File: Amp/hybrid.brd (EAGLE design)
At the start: 174 x 168.9 mm, 123 parts, among them IC1 TL071P, IC2 TL071P, IC3 LM317MABT-OUT, IC4 LM317MABT-OUT, J1 RCJ-21XXMILL, J2 NRJ3HF-1, J3 703W-00/54, Q1 BC560KINKED, Q10 BC560KINKED, Q11 BC560KINKED, Q12 BC560KINKED, Q13 BC556KINKED, Q14 BC550KINKED, Q15 BC550KINKED, Q16 BC560KINKED, Q17 BD140, Q18 BD139, Q19 KSP43, Q2 BC560KINKED, Q3 BC560KINKED, Q4 BC556KINKED, Q5 BC550KINKED, Q6 BC550KINKED, Q7 BC560KINKED, Q8 BD140, Q9 BD139, T1 TR-LP30-1600

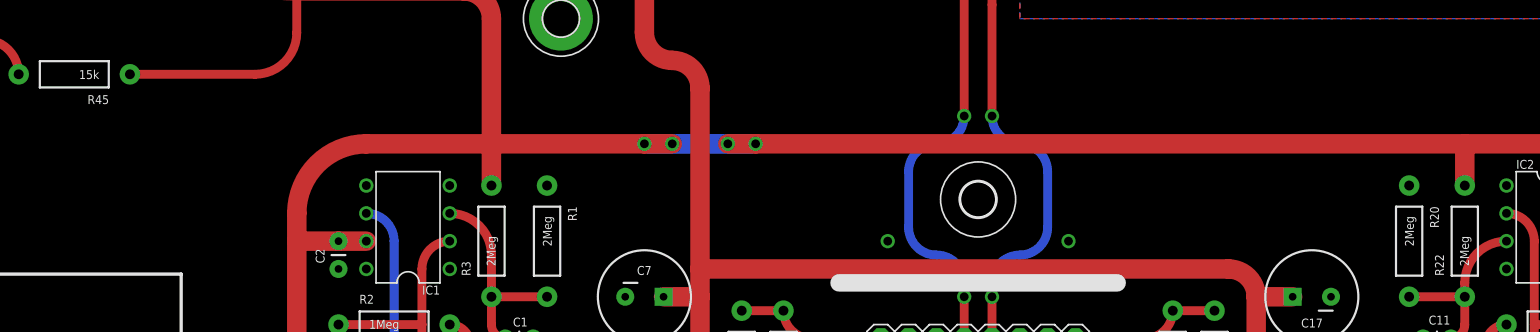
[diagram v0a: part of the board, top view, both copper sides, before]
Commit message: Improved auto biasing circuit
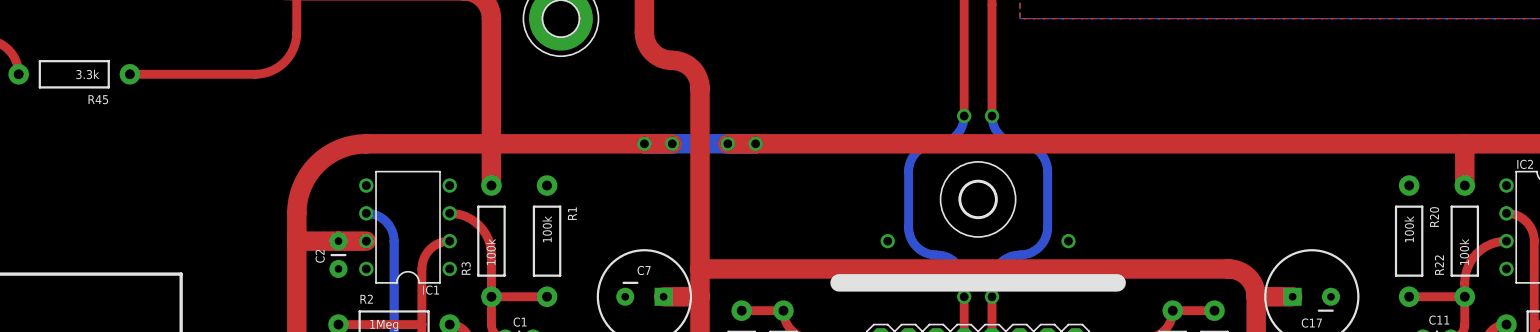
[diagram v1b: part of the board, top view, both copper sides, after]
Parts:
- R1, R20, R22, R3: value 2Meg -> 100k
- R45: value 15k -> 3.3k
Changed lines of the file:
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@@
 <?xml version="1.0" encoding="utf-8"?>
 <!DOCTYPE eagle SYSTEM "eagle.dtd">
-<eagle version="8.0.2">
+<eagle version="8.1.0">
 <drawing>
 <settings>
@@
 <attribute name="VALUE" x="46.355" y="1.143" size="0.8128" layer="27" ratio="20" rot="R180"/>
 </element>
-<element name="R1" library="SparkFun-Resistors" package="AXIAL-0.4" value="2Meg" x="57.15" y="67.31" smashed="yes" rot="R270">
+<element name="R1" library="SparkFun-Resistors" package="AXIAL-0.4" value="100k" x="57.15" y="67.31" smashed="yes" rot="R270">
 <attribute name="NAME" x="59.055" y="70.485" size="0.8128" layer="25" font="vector" ratio="20" rot="R270"/>
 <attribute name="VALUE" x="56.769" y="69.596" size="0.8128" layer="21" font="vector" ratio="20" rot="R270"/>
@@
 <attribute name="VALUE" x="37.719" y="26.416" size="0.8128" layer="21" font="vector" ratio="20" rot="R270"/>
 </element>
-<element name="R20" library="SparkFun-Resistors" package="AXIAL-0.4" value="2Meg" x="135.89" y="67.31" smashed="yes" rot="R270">
+<element name="R20" library="SparkFun-Resistors" package="AXIAL-0.4" value="100k" x="135.89" y="67.31" smashed="yes" rot="R270">
 <attribute name="NAME" x="137.795" y="70.485" size="0.8128" layer="25" font="vector" ratio="20" rot="R270"/>
 <attribute name="VALUE" x="135.509" y="69.596" size="0.8128" layer="21" font="vector" ratio="20" rot="R270"/>
@@
 <attribute name="VALUE" x="152.146" y="60.071" size="0.8128" layer="21" font="vector" ratio="20" rot="R180"/>
 </element>
-<element name="R22" library="SparkFun-Resistors" package="AXIAL-0.4" value="2Meg" x="140.97" y="67.31" smashed="yes" rot="R90">
+<element name="R22" library="SparkFun-Resistors" package="AXIAL-0.4" value="100k" x="140.97" y="67.31" smashed="yes" rot="R90">
 <attribute name="NAME" x="139.065" y="64.135" size="0.8128" layer="25" font="vector" ratio="20" rot="R90"/>
 <attribute name="VALUE" x="141.351" y="65.024" size="0.8128" layer="21" font="vector" ratio="20" rot="R90"/>
@@
 <attribute name="VALUE" x="154.559" y="26.416" size="0.8128" layer="21" font="vector" ratio="20" rot="R270"/>
 </element>
-<element name="R3" library="SparkFun-Resistors" package="AXIAL-0.4" value="2Meg" x="52.07" y="67.31" smashed="yes" rot="R90">
+<element name="R3" library="SparkFun-Resistors" package="AXIAL-0.4" value="100k" x="52.07" y="67.31" smashed="yes" rot="R90">
 <attribute name="NAME" x="50.165" y="64.135" size="0.8128" layer="25" font="vector" ratio="20" rot="R90"/>
 <attribute name="VALUE" x="52.451" y="65.024" size="0.8128" layer="21" font="vector" ratio="20" rot="R90"/>
@@
 <attribute name="VALUE" x="2.159" y="82.55" size="1.27" layer="27" ratio="10" rot="R270"/>
 </element>
-<element name="R45" library="SparkFun-Resistors" package="AXIAL-0.4" value="15k" x="13.97" y="82.55" smashed="yes" rot="R180">
+<element name="R45" library="SparkFun-Resistors" package="AXIAL-0.4" value="3.3k" x="13.97" y="82.55" smashed="yes" rot="R180">
 <attribute name="NAME" x="17.145" y="80.645" size="0.8128" layer="25" font="vector" ratio="20" rot="R180"/>
 <attribute name="VALUE" x="16.256" y="82.931" size="0.8128" layer="21" font="vector" ratio="20" rot="R180"/>

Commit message: Small changes
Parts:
- removed C30: 1uF, SparkFun-Capacitors:CAP-PTH-SMALL
- removed C31, C32: 47uF, my-cap:CPOL-RADIAL-8/3.5
- removed F1: (no value), fuse:SH22,5
- removed J1: RCJ-21XXMILL, my:RCJ-21-MILL
- removed J3: 703W-00/54, my-conn:703W-00/54
- removed S1: SW-M2012SA2W40, my-sw:SW-M2012S2A2G40
- removed T1: TR-LP30-1600, my-transformers:TR-LP30-1600
- removed U$1: ACRIDA-LOGO, my-logo:ACRIDA-LOGO
- removed U$2: (no value), my-logo:DANGER-LOGO
- added C25: 10uF, my-cap:CPOL-RADIAL-6.5/2.5
- added H1: MOUNT-PAD-ROUND3.2, holes:3,2-PAD
- added H6: MOUNT-HOLE3.2, holes:3,2
- added LOGO1: ACRIDA-LOGO, my-logo:ACRIDA-LOGO
- added Q20: BD139, transistor-npn:TO126
- added Q21, Q22: KSP43, my-tran:TO-92
- added R46: 23.7k, SparkFun-Resistors:AXIAL-0.4
- added R47: 3.3k, SparkFun-Resistors:AXIAL-0.4
- added R48: 220, SparkFun-Resistors:AXIAL-0.4
- added X1: (no value), con-wago-508:W237-3E
- added X2: (no value), con-wago-508:W237-2N
- C1, C11: value 0.1uF -> 1uF; device SparkFun-Capacitors:CAP-PTH-SMALL -> capacitor-wima:C5B5
- C10: value 470uF -> 1uF; device my-cap:CPOL-RADIAL-12.5/5 -> capacitor-wima:C5B5
- C12, C2: value 0.1uF -> 1uF
- C13: value 1uF -> 0.33u; device capacitor-wima:C5B5 -> capacitor-wima:C5B7.2
- C14: value 0.33u -> 100uF; device capacitor-wima:C5B3.5 -> my-cap:CPOL-RADIAL-8/3.5
- C15: value 10p -> 100uF; device SparkFun-Capacitors:CAP-PTH-SMALL -> my-cap:CPOL-RADIAL-12.5/5
- C16, C6: device my-cap:CPOL-RADIAL-8/3.5 -> my-cap:CPOL-RADIAL-12.5/5
- C17, C18, C8: value 47uF -> 470uF; device my-cap:CPOL-RADIAL-8/3.5 -> my-cap:CPOL-RADIAL-12.5/5
- C19, C20: device my-cap:CPOL-RADIAL-12.5/5 -> my-cap:CPOL-RADIAL-18/7.5
- C21: value 470uF -> 4700uF; device my-cap:CPOL-RADIAL-18/7.5 -> my-cap:CPOL-SNAPIN-30/10
- C22: value 470uF -> 1uF; device my-cap:CPOL-RADIAL-18/7.5 -> SparkFun-Capacitors:CAP-PTH-5MM
- C23: value 4700uF -> 47uF; device my-cap:CPOL-SNAPIN-30/10 -> my-cap:CPOL-RADIAL-12/5
- C24: value 1uF -> 10uF; device SparkFun-Capacitors:CAP-PTH-SMALL -> my-cap:CPOL-RADIAL-5/2.5
- C26: value 47uF -> 1uF; device my-cap:CPOL-RADIAL-12/5 -> SparkFun-Capacitors:CAP-PTH-SMALL
- C27: value 10uF -> 1uF; device my-cap:CPOL-RADIAL-5/2.5 -> SparkFun-Capacitors:CAP-PTH-SMALL
- C28: value 10uF -> 100uF; device my-cap:CPOL-RADIAL-6.5/2.5 -> my-cap:CPOL-RADIAL-12.5/5
- C29: value 1uF -> 100uF; device SparkFun-Capacitors:CAP-PTH-SMALL -> my-cap:CPOL-RADIAL-12.5/5
- C4: device capacitor-wima:C5B3.5 -> capacitor-wima:C5B7.2
- C5: value 10p -> 100uF; device SparkFun-Capacitors:CAP-PTH-SMALL -> my-cap:CPOL-RADIAL-8/3.5
- C7: value 47uF -> 100uF; device my-cap:CPOL-RADIAL-8/3.5 -> my-cap:CPOL-RADIAL-12.5/5
- H4: value MOUNT-PAD-ROUND3.2 -> MOUNT-HOLE3.2; device holes:3,2-PAD -> holes:3,2
- IC3, IC4: value LM317MABT-OUT -> LM317MABT; device my-reg:TO220L1-OUT -> my-reg:TO220L1
- Q1, Q11: value BC560KINKED -> KSP06KINKED
- Q10: value BC560KINKED -> BD139; device my-tran:TO92-BENT -> transistor-npn:TO126
- Q13, Q4: value BC556KINKED -> BC560KINKED
- Q14: value BC550KINKED -> BC560KINKED
- Q15, Q5: value BC550KINKED -> BC556KINKED
- Q16, Q7: value BC560KINKED -> BC550KINKED
- Q17: value BD140 -> BC550KINKED; device transistor-pnp:TO126 -> my-tran:TO92-BENT
- Q18: value BD139 -> BC560KINKED; device transistor-npn:TO126 -> my-tran:TO92-BENT
- Q19: value KSP43 -> BD140; device my-tran:TO-92 -> transistor-pnp:TO126
- Q8: value BD140 -> BC560KINKED; device transistor-pnp:TO126 -> my-tran:TO92-BENT
- Q9: value BD139 -> BD140; device transistor-npn:TO126 -> transistor-pnp:TO126
- R1: value 100k -> 1Meg
- R10, R30: value 2.2k -> 4.7k
- R12, R31: value 10k -> 2.2k
- R13: value 4.7k -> 10k
- R14: value 10k -> 4.7k; device SparkFun-Electromechanical:3362U-2 -> SparkFun-Resistors:AXIAL-0.4
- R15, R35: value 220 -> 10k; device SparkFun-Resistors:AXIAL-0.4 -> SparkFun-Electromechanical:3362U-2
- R17, R36, R37: value 2.2 -> 220
- R19, R38: value 2.2k -> 2.2
- R2: value 1Meg -> 2Meg
- R20: value 100k -> 2.2k
- R22, R3: value 100k -> 2Meg
- R23: value 330 -> 2Meg
- R24: value 27k -> 1Meg
- R25, R6: value 1Meg -> 330
- R27: value 820 -> 5.1k
- R28: value 4.7k -> 330
- R29: value 2.2k -> 820
- R32: value 4.7k -> 2.2k
- R33: device SparkFun-Electromechanical:3362U-2 -> SparkFun-Resistors:AXIAL-0.4
- R34: value 220 -> 4.7k
- R39: value 0.51 -> 2.2; device my-res:AXIAL-0.5 -> SparkFun-Resistors:AXIAL-0.4
- R4: value 330 -> 1Meg
- R41: value 240 -> 0.51; device SparkFun-Resistors:AXIAL-0.4 -> my-res:AXIAL-0.5
- R42: value 5.49k -> 2.2k
- R43: value 510 -> 240
- R44: value 23.7k -> 5.49k
- R45: value 3.3k -> 510
- R5: value 27k -> 330
- R7: value 330 -> 5.1k
- R8: value 820 -> 330
- R9: value 4.7k -> 820
- V1: device my-tubes:NOVAL-HORIZONTAL -> my-tubes:NOVAL-21MM
- moved R40 165.4 mm to (146.1, 12.7), turned to 270 degrees
- moved R45 150.2 mm to (161.3, 111.8), turned to 90 degrees
- moved Q19 149.6 mm to (171.4, 40.6), turned to 270 degrees
- moved C29 143.0 mm to (147.3, 104.1), turned to 0 degrees
- moved Q10 139.1 mm to (1.27, 22.9), turned to 90 degrees
- moved C27 138.0 mm to (149.9, 116.8), turned to 180 degrees
- moved IC4 132.4 mm to (170.2, 111.8), turned to 270 degrees
- moved VR1 127.9 mm to (115.6, -1.27), turned to 270 degrees
- moved D6 125.8 mm to (161.3, 121.9), turned to 0 degrees
- moved D3 117.1 mm to (161.3, 101.6), turned to 180 degrees
- moved H2 115.0 mm to (86.4, 5.08)
- moved R42 114.4 mm to (125.7, 109.2), turned to 90 degrees
- moved C23 114.4 mm to (130.8, 121.9), turned to 270 degrees
- moved R39 107.3 mm to (157.5, 16.5), turned to 180 degrees
- moved C20 107.2 mm to (110.5, 114.3), turned to 270 degrees
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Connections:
- removed net N$40: F1.1, J3.L
- removed net N$44: F1.2, S1.S
- removed net N$45: S1.UP-CONNECT, T1.4
- removed net P$1: J3.E
- new net N$47: Q1.1, R7.P$2
- new net N$48: Q11.1, R27.P$2
- net +6.3FIL: now also R41.P$2, V1.4; no longer R39.P$2, V1.7, V1.8
- net +LV: now also C21.1; no longer C23.1
- net AC_1: now also X2.2; no longer T1.8
- net AC_2: now also C19.2, X2.1; no longer C21.2, T1.5
- net CAT_L: now also R10.P$2, V1.3; no longer R8.P$2, V1.2
- net CAT_R: now also R29.P$2, R30.P$2, V1.8; no longer R27.P$2, R28.P$2, V1.16
- net FB_L: now also C5.2, C8.+, R1.P$2, R18.P$1, R19.P$2; no longer C10.+, C6.2, R17.P$1, R18.P$2, R2.P$2
- net FB_R: now also C14.2, C17.+, C18.+, R38.P$1, R39.P$2; no longer C16.2, C19.+, C20.+, R36.P$1, R37.P$2
- net FGND: now also V1.5; no longer V1.10, V1.9
- net GND: now also C10.1, C15.-, C16.-, C20.2, C21.2, C23.-, C25.2, C26.2, C28.-, C29.-, C6.-, C7.-, H1.B3,2, Q10.1, Q20.1, R12.P$1, R17.P$1, R23.P$2, R24.P$1, R29.P$1, R3.P$2, R32.P$1, R37.P$1, R4.P$1, R40.P$1, R46.P$2, R7.P$1, R9.P$1, X1.2; no longer C11.1, C17.2, C18.2, C23.2, C26.-, C28.2, C29.2, C30.2, C31.2, C32.2, C7.2, C8.2, H4.B3,2, J1.1, J1.3, Q18.1, Q9.1, R1.P$1, R11.P$1, R16.P$1, R19.P$1, R25.P$1, R30.P$1, R35.P$1, R38.P$1, R42.P$2, R6.P$1, R8.P$1, V1.11, V1.12, V1.14, V1.4, V1.5, V1.6
- net G_L: now also R4.P$2, R5.P$2; no longer R6.P$2, V1.3
- net G_R: now also C13.2, R24.P$2; no longer C14.2, V1.13
- net HT: now also C15.+, C29.+, C6.+, R11.P$2, R28.P$2, R31.P$2, R45.P$1, R6.P$2, R8.P$2; no longer C17.1, C32.1, C7.1, R10.P$2, R23.P$2, R29.P$2, R4.P$2, R43.P$1, R7.P$2
- net IN_L: now also VR1.1.2; no longer VR1.2.2.1, VR1.2.2.2
- net IN_L*: now also VR1.1.3.1, VR1.1.3.2, X1.1; no longer J1.4, VR1.2.3.1, VR1.2.3.2
- net IN_R: now also C13.1, VR1.2.2.1, VR1.2.2.2; no longer C14.1, VR1.1.2
- net IN_R*: now also VR1.2.3.1, VR1.2.3.2, X1.3; no longer J1.2, VR1.1.3.1, VR1.1.3.2
- net ISET_L: now also Q1.3, Q2.1, Q4.2; no longer Q1.1, Q3.2, R5.P$2
- net ISET_R: now also Q11.3, Q12.1, Q14.2; no longer Q10.1, Q12.2, R24.P$2
- net N$1: now also Q3.1, Q3.2, Q4.3; no longer Q1.2, Q2.1, Q3.3
- net N$10: now also R14.P$2, R15.3; no longer R13.P$2, R14.3
- net N$11: now also Q7.3, Q9.2, R18.P$2; no longer Q6.3, Q8.2, R17.P$2
- net N$12: now also Q6.3, Q8.2, R12.P$2, R15.1, R15.2; no longer Q5.3, Q7.2, R11.P$2, R14.1, R14.2
- net N$13: now also Q10.2, Q8.3, R19.P$1; no longer Q7.3, Q9.2, R18.P$1
- net N$14: now also Q7.1, Q9.3, R16.P$1; no longer Q6.1, Q8.3, R15.P$1
- net N$15: now also Q10.3, Q8.1, R17.P$2; no longer Q7.1, Q9.3, R16.P$2
- net N$16: now also Q13.3, R28.P$1; no longer Q11.3, R26.P$1
- net N$17: now also Q12.2, Q13.1, Q13.2, Q14.3; no longer Q10.2, Q11.1, Q11.2, Q12.3
- net N$18: now also Q21.2, Q22.1, R48.P$2; no longer J3.N, T1.1
- net N$19: now also C14.1, R30.P$1; no longer C16.1, R28.P$1
- net N$2: now also Q3.3, R8.P$1; no longer Q2.3, R7.P$1
- net N$20: now also Q15.3, R31.P$1; no longer Q13.3, R29.P$1
- net N$21: now also Q15.1, Q16.1, Q17.2, R33.P$2; no longer C15.2, Q13.1, Q14.1, Q15.2, R31.P$2
- net N$22: now also Q16.2, R33.P$1, R34.P$1; no longer Q14.2, R31.P$1, R32.P$1
- net N$23: now also R34.P$2, R35.3; no longer R32.P$2, R33.3
- net N$24: now also Q16.3, Q18.2, R32.P$2, R35.1, R35.2; no longer Q14.3, Q16.2, R30.P$2, R33.1, R33.2
- net N$25: now also Q17.3, Q19.2, R38.P$2; no longer Q15.3, Q17.2, R36.P$2
- net N$26: now also Q18.3, Q20.2, R39.P$1; no longer Q16.3, Q18.2, R37.P$1
- net N$27: now also Q17.1, Q19.3, R36.P$1; no longer Q15.1, Q17.3, R34.P$1
- net N$28: now also Q18.1, Q20.3, R37.P$2; no longer Q16.1, Q18.3, R35.P$2
- net N$29: now also Q1.2; no longer R5.P$1
- net N$3: now also Q2.3, R6.P$1; no longer Q1.3, R4.P$1
- net N$30: now also C24.1, C26.1, R43.P$2, R44.P$1; no longer C27.1, C29.1, R41.P$2, R42.P$1
- net N$31: now also C19.1; no longer C21.1
- net N$32: now also R41.P$1; no longer R39.P$1
- net N$33: now also C20.1, Q21.3, Q22.3, R42.P$1; no longer C22.1, Q19.3, R40.P$1
- net N$34: now also C22.1, C23.+, Q22.2, R42.P$2; no longer C24.1, C26.+, Q19.2, R40.P$2
- net N$35: now also R3.P$1
- net N$36: now also C25.1, C27.1, R45.P$2, R46.P$1; no longer C28.1, C30.1, R43.P$2, R44.P$1
- net N$37: now also Q21.1, R48.P$1; no longer Q19.1
- net N$38: now also R1.P$1; no longer R1.P$2, R3.P$1
- net N$39: now also Q12.3, R26.P$1; no longer Q10.3, R23.P$1
- net N$4: now also C5.1, R10.P$1; no longer C6.1, R9.P$1
- net N$41: now also C11.2, IC2.2, R22.P$1, R23.P$1; no longer C13.1, IC2.6, R24.P$1
- net N$42: now also C10.2, IC2.3; no longer C13.2, IC2.2
- net N$43: now also C11.1, IC2.6, Q11.2; no longer C11.2, IC2.3, R20.P$2, R22.P$1
- net N$46: now also R47.P$2; no longer R45.P$2
- net N$5: now also Q5.3, R11.P$1; no longer Q4.3, R10.P$1
- net N$6: now also R5.P$1, V1.2; no longer T1.2, T1.3
- net N$7: now also Q6.1, Q7.2, R13.P$2; no longer C5.2, Q4.1, Q6.2, R12.P$2
- net N$8: now also Q6.2, R14.P$1; no longer Q5.2, R12.P$1
- net N$9: now also R25.P$1, V1.7; no longer T1.6, T1.7
- net OUT_L: now also C8.-, R20.P$2; no longer C10.-, R19.P$2
- net OUT_R: now also C17.-, C18.-, R40.P$2; no longer C19.-, C20.-, R38.P$2
- net PL_L: now also Q4.1, Q5.2; no longer C5.1, Q3.1, Q4.2
- net PL_R: now also Q14.1, Q15.2, V1.6; no longer C15.1, Q12.1, Q13.2, V1.15
- net VCC: now also C16.+, C28.+, C7.+, Q19.1, Q9.1, R16.P$2, R2.P$2, R36.P$2, R43.P$1, R47.P$1; no longer C18.1, C31.1, C8.1, Q17.1, Q8.1, R15.P$2, R3.P$2, R34.P$2, R41.P$1, R45.P$1
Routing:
- net IN_L*: track 212.2 -> 32.3 mm
- net IN_R*: track 201.4 -> 31.5 mm
- net VCC: track 567.3 -> 422.7 mm, vias 7 -> 0
- net IN_R: track 155.5 -> 39.9 mm, vias 2 -> 0
- net IN_L: track 118.7 -> 51.4 mm, vias 3 -> 0
- net N$40: track 57.2 -> 0.00 mm
- net N$45: track 55.1 -> 0.00 mm
- net HT: track 228.9 -> 282.5 mm, vias 2 -> 4
- net +LV: track 152.3 -> 98.8 mm
- net OUT_R: track 165.2 -> 114.3 mm, vias 1 -> 3
- net N$44: track 42.4 -> 0.00 mm
- net N$18: track 49.1 -> 12.4 mm
- net N$6: track 39.2 -> 6.60 mm
- net N$9: track 38.1 -> 6.60 mm
- net G_R: track 40.1 -> 12.8 mm
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- removed copper zone on layer 1, net N$31
- removed copper zone on layer 1, net N$33
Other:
- board size 174 x 168.9 mm -> 172.7 x 137.2 mm
- board text added: "30VAC"
- board text added: "G"
- board text added: "L"
- board text added: "R"

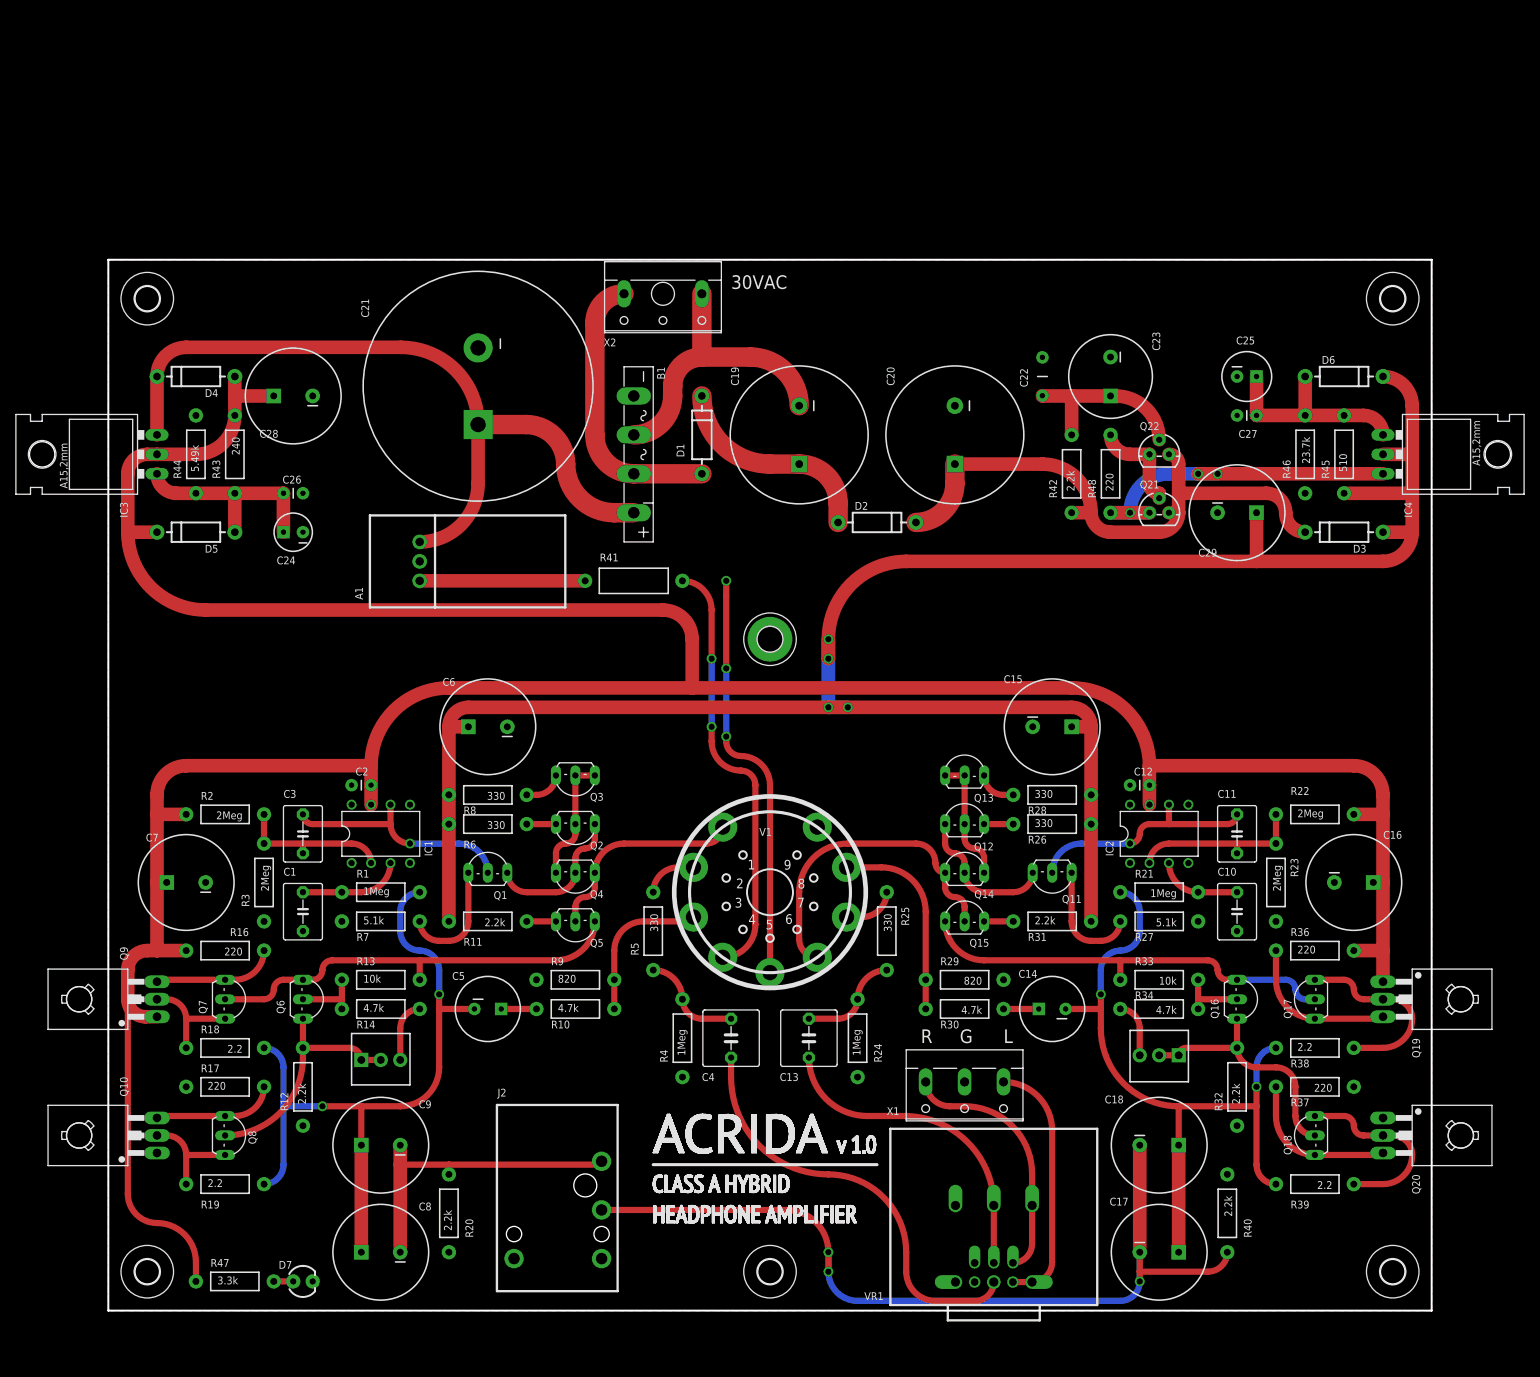
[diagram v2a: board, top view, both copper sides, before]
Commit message: Ground plane on top
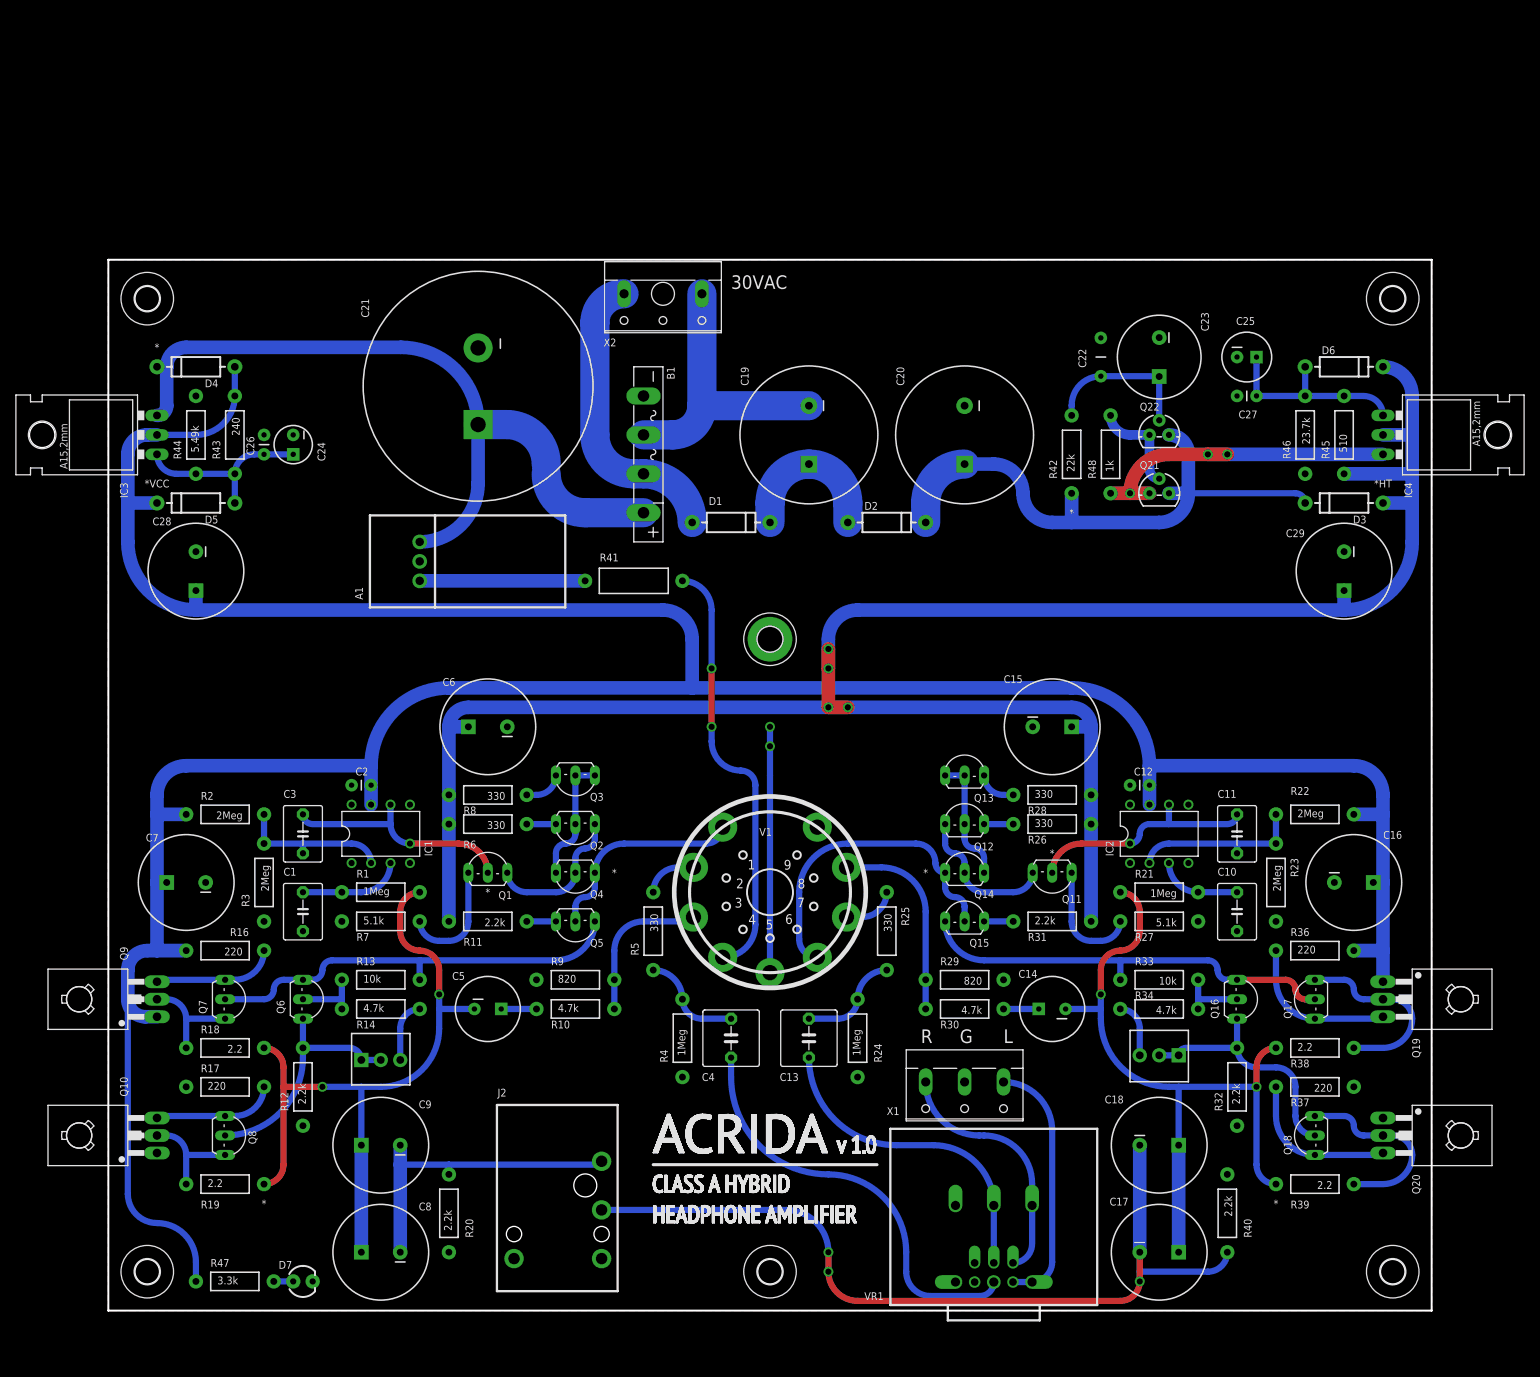
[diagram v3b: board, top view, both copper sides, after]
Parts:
- C23: value 47uF -> 10uF
- R42: value 2.2k -> 22k
- R48: value 220 -> 1k
- moved C28 26.2 mm to (11.4, 96.5), turned to 270 degrees
- moved GB1 24.2 mm to (86.4, 69.8), flipped to the bottom
- moved C29 15.9 mm to (161.3, 96.5), turned to 270 degrees
- moved D1 12.0 mm to (81.3, 102.9), turned to 0 degrees
- moved C24 11.4 mm to (24.1, 113.0), turned to 270 degrees
- moved C22 8.03 mm to (129.5, 124.5)
- moved C23 6.84 mm to (137.2, 124.5)
- moved C26 5.68 mm to (20.3, 111.8), turned to 90 degrees
- moved D3 3.81 mm to (161.3, 105.4)
- moved D5 3.81 mm to (11.4, 105.4)
- moved Q21 2.54 mm to (137.2, 106.7)
- moved R42 2.54 mm to (125.7, 111.8)
- moved R48 2.54 mm to (130.8, 111.8)
- moved C25 2.54 mm to (148.6, 124.5)
- moved C27 2.54 mm to (149.9, 119.4)
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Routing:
- net FGND: track 51.6 -> 25.7 mm, vias 2 -> 0
- net N$31: track 26.1 -> 19.4 mm
- net GND: track 1.91 -> 6.35 mm, vias 1 -> 2
- net N$30: track 27.7 -> 23.7 mm
- net N$34: track 22.7 -> 20.0 mm
- net HT: track 282.5 -> 280.7 mm
- net FB_L: track 92.0 -> 90.5 mm
- net AC_1: track 36.1 -> 37.4 mm
- net N$36: track 27.7 -> 26.5 mm
- net IN_R*: track 31.5 -> 30.8 mm
- net FB_R: track 89.0 -> 89.7 mm
- net +LV: track 98.8 -> 99.6 mm
- net IN_L: track 51.4 -> 50.9 mm
- net VCC: track 422.7 -> 422.2 mm
- removed copper zone on layer 16, net GND
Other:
- board text added: "*"
- board text added: "*HT"
- board text added: "*VCC"
